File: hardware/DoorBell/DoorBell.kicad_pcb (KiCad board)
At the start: 2 copper layers, 83.8 x 110.5 mm, 37 parts, among them J1 Barrel_Jack_Switch_Pin3Ring, J2 USB_A, J3 Speaker, J4 ARDUINO_IO, J5 DFPlayerIO, P1 Digital, P2 COM, P3 ADC, P4 Analog, P5 ADC, SW1 DoorBell, SW2 Volume Up, SW3 Volume Down, SW4 Select, SW5 Next, SW6 Prev, U1 DFPLAYER_MINI

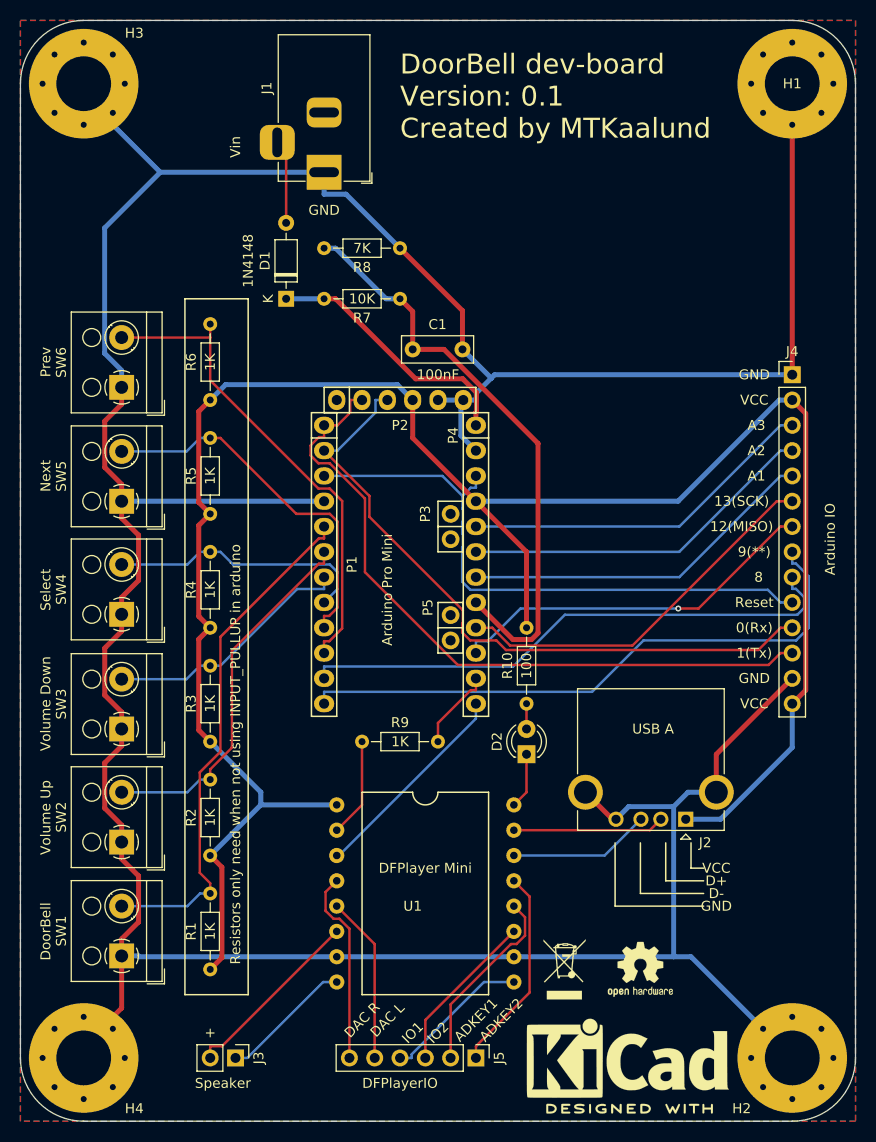
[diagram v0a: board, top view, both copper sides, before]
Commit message: Added a low voltage led to the board on pin 9.
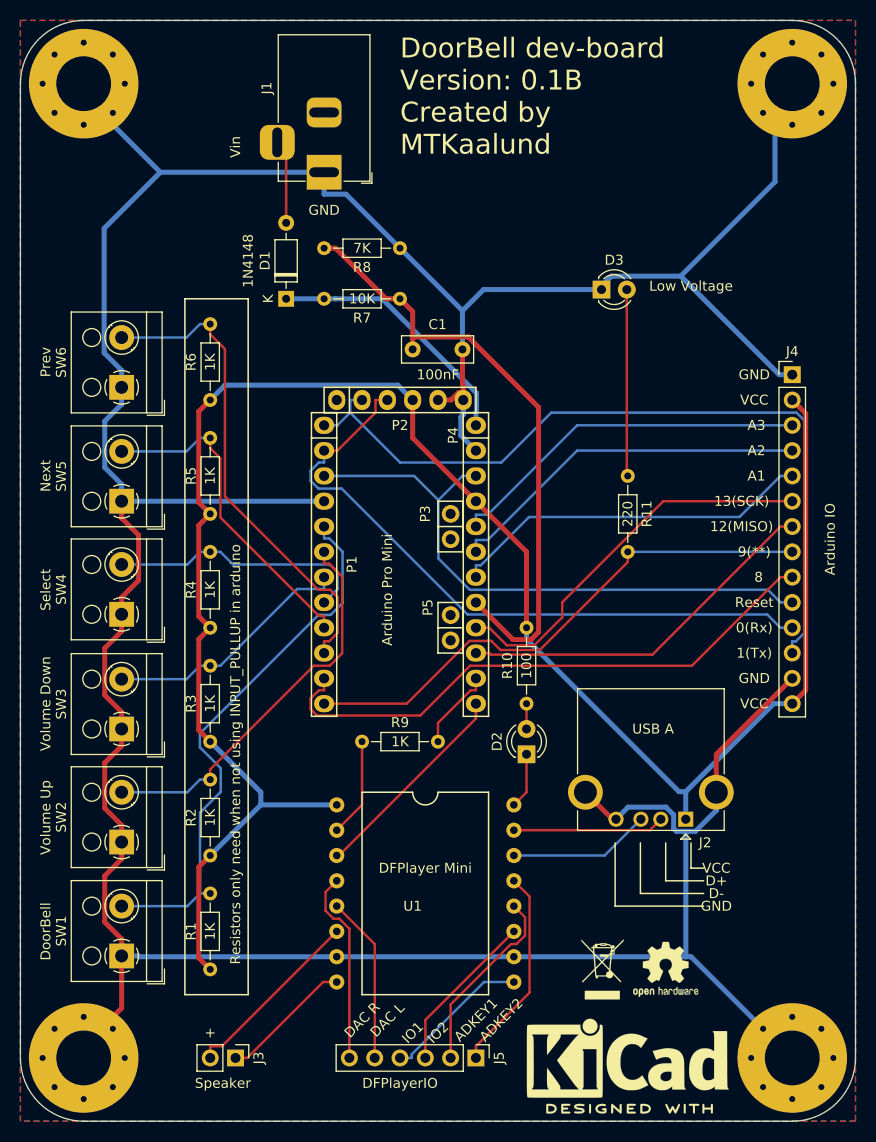
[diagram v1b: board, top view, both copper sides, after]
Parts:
- added D3: LowBatteryLED, LED_THT:LED_D3.0mm, F.Cu at (166.3, 71.5)
- added R11: 220, Resistor_THT:R_Axial_DIN0204_L3.6mm_D1.6mm_P7.62mm_Horizontal, F.Cu at (168.9, 90.2)
- moved LOGO2 3.81 mm to (166.4, 139.7)
- moved LOGO3 2.54 mm to (172.7, 139.7)
- renumbered REF** to LOGO1, REF** to LOGO2, REF** to LOGO3
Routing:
- net Net-(D3-Pad2): track 0.00 -> 18.7 mm
- net VCC: track 207.6 -> 194.1 mm
- net /1(Tx): track 71.4 -> 79.7 mm
- net /9(**): track 61.0 -> 54.7 mm
- net Pin6: track 37.2 -> 33.5 mm
- net Pin2: track 52.2 -> 55.7 mm
- net /8: track 55.6 -> 58.3 mm
- net PWR_MON: track 58.9 -> 61.6 mm
- net Pin3: track 37.3 -> 39.8 mm
- net GND: track 458.2 -> 459.6 mm
- net /13(SCK): track 38.5 -> 39.4 mm
- net /A1: track 36.0 -> 36.7 mm
- net /A3: track 36.0 -> 36.7 mm
- net /A2: track 36.0 -> 36.7 mm
- net /12(MISO): track 37.7 -> 37.1 mm, vias 1 -> 0
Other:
- board text added: "220"
- board text added: "DoorBell dev-board Version: 0.1B Created by MTKaalund"
- board text added: "Low Voltage"
- board text removed: "DoorBell dev-board Version: 0.1 Created by MTKaalund"

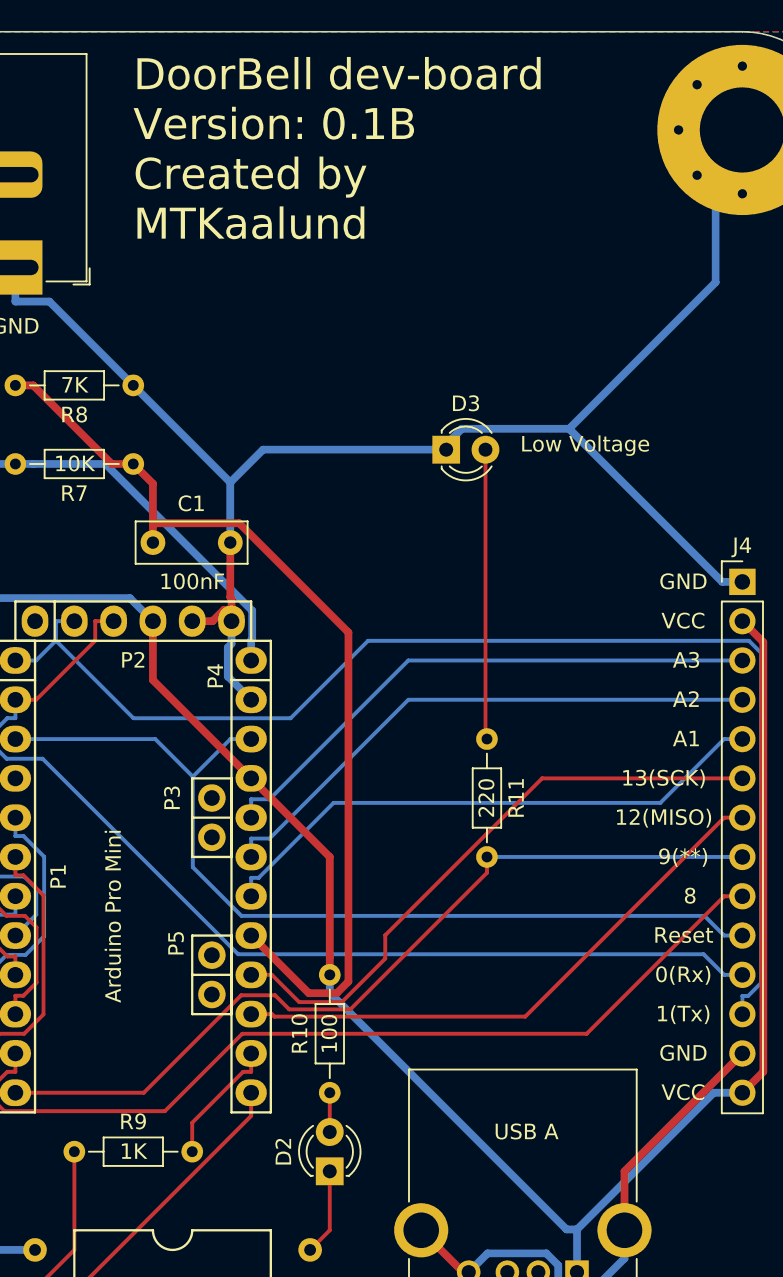
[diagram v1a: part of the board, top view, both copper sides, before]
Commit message: Updated silkscreen
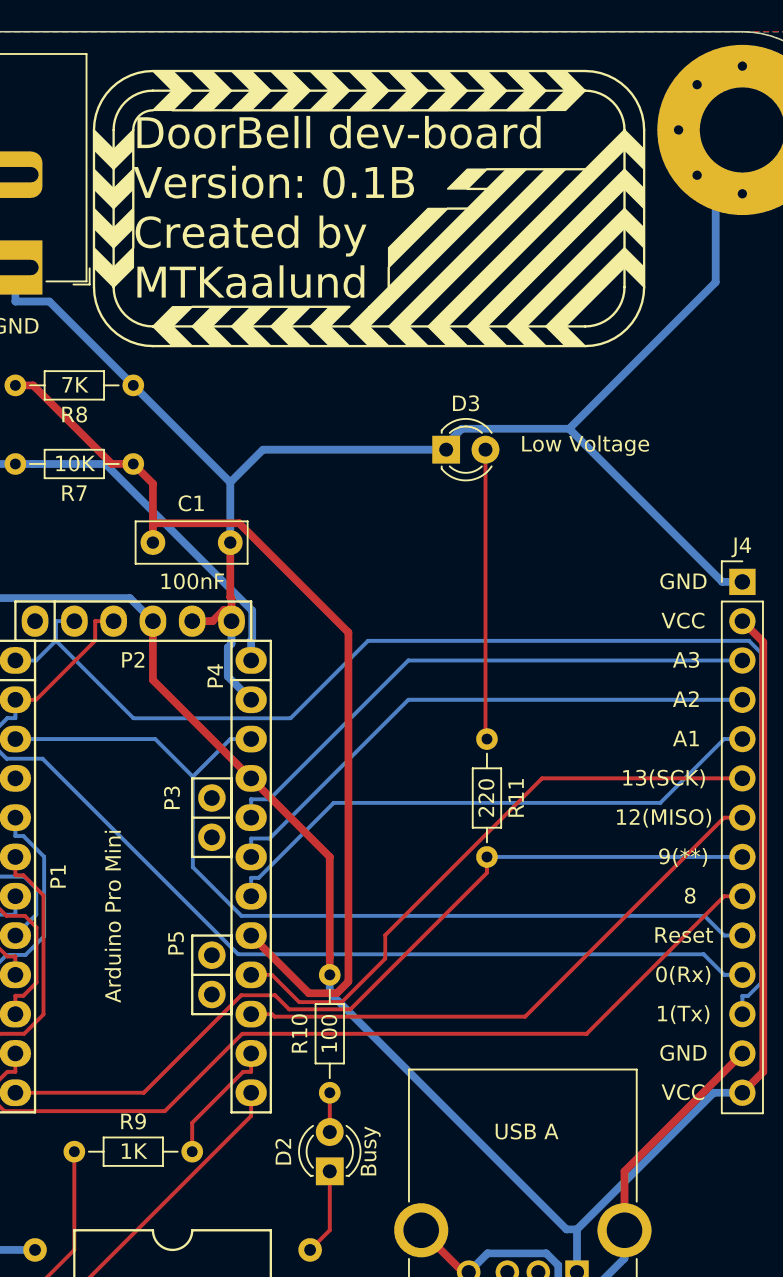
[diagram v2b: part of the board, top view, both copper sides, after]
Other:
- board text added: "Busy"
